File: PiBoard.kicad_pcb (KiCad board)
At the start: 4 copper layers, 90.1 x 92.5 mm, 128 parts, among them IC1 TCAN337DCNR, IC2 TPS2553QDBVRQ1, IC3 LM74502HDDFR, IC4 AP64501QSP-13, IC5 74LVC1G07QSE-7, IC6 TPS2553QDBVRQ1, IC7 TPS2553QDBVRQ1, J1 CarLVPowerConnector, J12 RTC Battery Port, J3 2222, J4 USB_C_Receptacle_USB2.0_16P, J5 USB_C_Receptacle_USB2.0_16P, J6 CarCANConnector, J7 Molex 470531000, J8 CarCANConnector, J9 HDMI_E, Q1 PSMN8R5-40MSDX, SW1 SW_Push, SW2 SW_Push, SW3 SW_Push, U1 RTC PCF8563T, U10 Fan PWM Controller, U13 CDSOT23-T24CAN, U14 MCP2515-E/STVAO, U3 FSUSB42MUX, Y4 8 MHz, Y6 ECS-.327-6

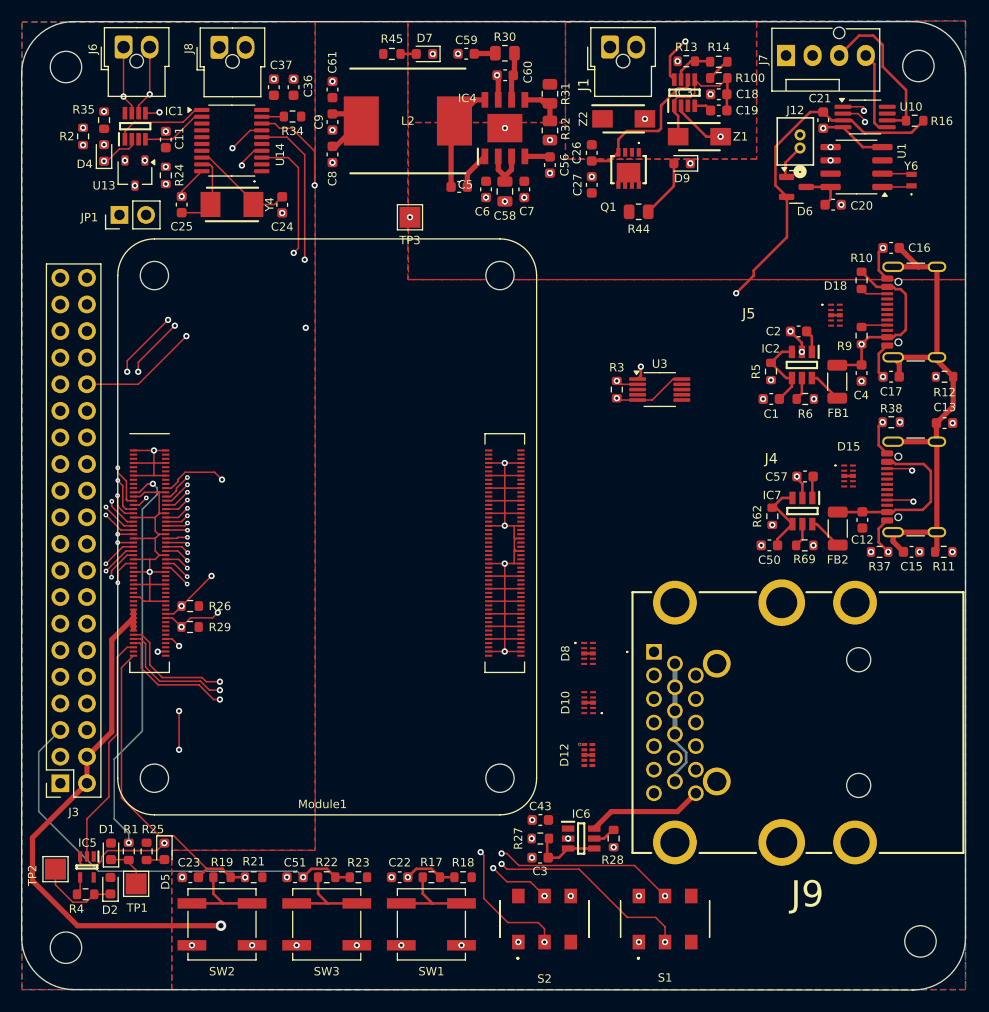
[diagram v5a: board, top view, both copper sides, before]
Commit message: ready to route high speed i believe
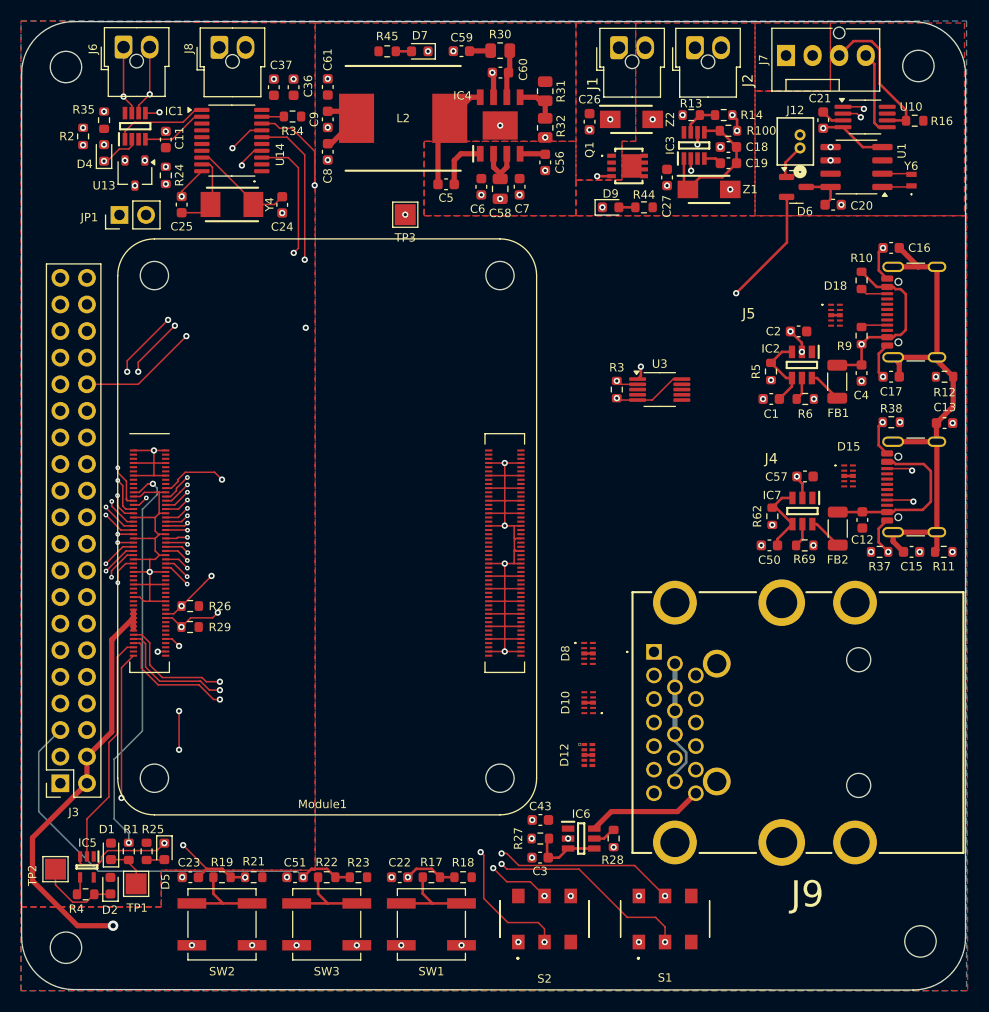
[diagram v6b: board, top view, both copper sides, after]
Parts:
- added J2: Display Breakout, UTSVT_Connectors:Molex_Nano-Fit_105309-xx02_1x02_P2.50mm_Vertical, F.Cu at (166.1, 53.8)
- R44: footprint Resistor_SMD:R_0805_2012Metric -> Resistor_SMD:R_0603_1608Metric
- moved D9 8.01 mm to (158.0, 69.0), turned to 0 degrees
- moved C27 7.22 mm to (163.4, 66.2), turned to -90 degrees
- moved R13 5.16 mm to (165.7, 60.2)
- moved IC3 5.12 mm to (166.0, 63.1)
- moved R100 5.12 mm to (169.3, 61.7), turned to 180 degrees
- moved C18 5.12 mm to (169.3, 63.2)
- moved C19 5.12 mm to (169.3, 64.8)
- moved Z1 5.12 mm to (167.4, 67.3)
- moved R14 5.11 mm to (168.8, 60.2)
- moved C26 2.98 mm to (156.0, 60.8)
- moved C5 1.27 mm to (142.3, 66.8)
- moved J1 0.86 mm to (158.8, 53.8)
- moved Z2 0.74 mm to (160.0, 60.6)
- moved R44 0.67 mm to (161.2, 69.0), turned to 180 degrees
- moved C56 0.51 mm to (151.8, 64.7)
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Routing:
- net +3.3V: track 80.2 -> 60.4 mm
- net +24V: track 22.0 -> 4.83 mm, vias 1 -> 0
- net +5V: track 61.6 -> 47.3 mm
- net GND: track 179.5 -> 175.4 mm, vias 70 -> 71
- net Net-(D9-A): track 5.64 -> 1.57 mm
- net Net-(IC3-GATE): track 14.8 -> 18.1 mm, vias 0 -> 3
- net /CM4 GPIO/SCL0: track 102.0 -> 99.3 mm
- net Net-(IC4-BST): track 3.61 -> 5.03 mm
- net /CM4 GPIO/SDA0: track 106.7 -> 105.3 mm
- net Net-(J7-Pin_3): track 15.3 -> 14.4 mm
- net /Power Distribution/LV+: track 2.29 -> 1.69 mm, vias 0 -> 3
- net Net-(IC3-OV): track 4.00 -> 3.46 mm
- net /Board_En: vias 4 -> 6
- added copper zone on In2.Cu, net /Power Distribution/LV+

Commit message: changed a bunch of stuff, still have work
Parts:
- removed C50, C57: 100n, Capacitor_SMD:C_0603_1608Metric
- removed IC7: TPS2553QDBVRQ1, Controls_Pi:SOT95P280X145-6N
- removed R62: 100n, Resistor_SMD:R_0603_1608Metric
- removed R69: 82k, Resistor_SMD:R_0603_1608Metric
- added C10: 120uF, Capacitor_SMD:C_0603_1608Metric, F.Cu at (179.7, 82.5)
- added C14: 100n, Capacitor_SMD:C_0603_1608Metric, F.Cu at (177.2, 98.9)
- added C28: 22uF, Capacitor_SMD:C_0603_1608Metric, F.Cu at (173.1, 96.5)
- added C29: 100uF, Capacitor_SMD:C_0805_2012Metric, F.Cu at (155.4, 125.2)
- added D11: VBUS_Debug LED, LED_SMD:LED_0603_1608Metric, F.Cu at (166.5, 102.3)
- added D3: VBUS_Hub LED, LED_SMD:LED_0603_1608Metric, F.Cu at (175.7, 90.0)
- added IC8: TPS25200DRVR, UTSVT_Power:SON65P200X200X80-7N, F.Cu at (173.1, 98.7)
- added R15: 33k, Resistor_SMD:R_0603_1608Metric, F.Cu at (169.9, 99.3)
- added R20: 100k, Resistor_SMD:R_0603_1608Metric, F.Cu at (175.6, 98.9)
- added R33: 100k, Resistor_SMD:R_0603_1608Metric, F.Cu at (173.0, 100.8)
- added R7: 1.5k, Resistor_SMD:R_0603_1608Metric, F.Cu at (179.0, 90.0)
- added R8: 1.5k, Resistor_SMD:R_0603_1608Metric, F.Cu at (169.7, 102.3)
- added TP4: TestPoint, TestPoint:TestPoint_Pad_2.0x2.0mm, F.Cu at (125.4, 128.5)
- C24, C25: value 22 pF -> 26 pF
- C6: value 100n -> 10uF
- R10, R9: value 5.1k -> 56k
- R5: value 100n -> 100k
- R6: value 82k -> 56k
- moved Y4 5.88 mm to (117.7, 64.6), turned to -90 degrees
- moved C24 5.14 mm to (121.9, 66.9), turned to 180 degrees
- moved C25 4.82 mm to (121.9, 68.5), turned to 180 degrees
- moved U14 2.31 mm to (124.2, 62.6)
- moved R34 1.54 mm to (128.9, 59.4), turned to 90 degrees
- moved D4 1.35 mm to (108.3, 63.8)
- moved R35 1.35 mm to (108.3, 60.7)
- moved R2 1.35 mm to (106.3, 62.2)
- moved C11 1.35 mm to (114.2, 62.5)
- moved IC1 1.35 mm to (111.3, 61.3)
- moved JP1 1.35 mm to (109.8, 69.7)
- moved U13 1.35 mm to (111.2, 65.7)
- moved R24 1.35 mm to (114.2, 66.0)
- moved R9 0.55 mm to (182.0, 81.8), turned to -90 degrees
- moved C36 0.47 mm to (127.3, 57.5)
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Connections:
- C4 pad 1: Net-(C4-Pad1) -> Net-(C10-Pad1)
- FB1 pad 2: Net-(C4-Pad1) -> Net-(C10-Pad1)
- J5 pad A4: Net-(C4-Pad1) -> Net-(C10-Pad1)
- J5 pad A9: Net-(C4-Pad1) -> Net-(C10-Pad1)
- J5 pad B4: Net-(C4-Pad1) -> Net-(C10-Pad1)
- J5 pad B9: Net-(C4-Pad1) -> Net-(C10-Pad1)
- Module1 pad 88: unconnected-(Module1A-+1.8v_(Output)-Pad88) -> +1.8V
- Module1 pad 90: unconnected-(Module1A-+1.8v_(Output)-Pad90) -> +1.8V
- R10 pad 1: Net-(C4-Pad1) -> +5V
- R9 pad 1: Net-(C4-Pad1) -> +5V
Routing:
- net +3.3V: track 60.4 -> 90.1 mm, vias 3 -> 4
- net +1.8V: track 0.00 -> 26.8 mm
- net Net-(C4-Pad1): track 17.6 -> 0.00 mm, vias 1 -> 0
- net Net-(C10-Pad1): track 0.00 -> 15.8 mm
- net /USB2.0 high speed/VBUS_Debug: track 3.25 -> 16.8 mm
- net Net-(IC7-EN): track 7.51 -> 0.00 mm
- net /CM4 GPIO/CAN_SPI_MISO: track 86.5 -> 92.3 mm
- net /CarCAN/CAN_RX: track 6.28 -> 9.96 mm
- net /CarCAN/CAN_TX: track 8.94 -> 12.6 mm
- net Net-(J5-CC1): track 2.52 -> 5.59 mm, vias 0 -> 2
- net /Board_En: track 129.2 -> 126.2 mm, vias 6 -> 5
- net /USB2.0 high speed/VBUS_Hub: track 3.22 -> 6.08 mm
- net /HDMI and High Speed/HDMI_5V: track 11.1 -> 13.6 mm
- net Net-(IC7-ILIM): track 2.28 -> 0.00 mm
- net /CM4 GPIO/CAN_INTR: track 51.8 -> 49.8 mm
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
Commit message: poop
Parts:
- removed C14: 100n, Capacitor_SMD:C_0603_1608Metric
- removed C28: 22uF, Capacitor_SMD:C_0603_1608Metric
- removed IC8: TPS25200DRVR, UTSVT_Power:SON65P200X200X80-7N
- added C30: 100n, Capacitor_SMD:C_0603_1608Metric, F.Cu at (177.4, 98.8)
- added C31: 100n, Capacitor_SMD:C_0603_1608Metric, F.Cu at (170.7, 97.8)
- added D13: HBT, LED_SMD:LED_0603_1608Metric, F.Cu at (159.7, 76.4)
- added D14: FAULT, LED_SMD:LED_0603_1608Metric, F.Cu at (159.7, 74.7)
- added D16: STUFF, LED_SMD:LED_0603_1608Metric, F.Cu at (159.7, 78.1)
- added IC7: TPS2553QDBVRQ1, Controls_Pi:SOT95P280X145-6N, F.Cu at (174.4, 98.5)
- added R36: 0, Resistor_SMD:R_0603_1608Metric, F.Cu at (174.3, 101.1)
- added R39: 100k, Resistor_SMD:R_0603_1608Metric, F.Cu at (170.7, 96.2)
- added R40: 56k, Resistor_SMD:R_0603_1608Metric, F.Cu at (170.7, 99.6)
- R15: value 33k -> 700
- R20, R33: value 100k -> 700
- moved R20 30.8 mm to (156.5, 74.7), turned to 180 degrees
- moved R33 28.1 mm to (156.5, 78.1), turned to 180 degrees
- moved R15 26.6 mm to (156.5, 76.4), turned to 180 degrees
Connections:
- R15 pad 1: GND -> Net-(D13-K)
- R15 pad 2: Net-(IC8-ILIM) -> /CM4 GPIO/GPIO19
- R20 pad 2: /USB2.0 high speed/VBUS_Debug -> /CM4 GPIO/GPIO13
- R33 pad 2: +3.3V -> /CM4 GPIO/GPIO26
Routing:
- net /CM4 GPIO/GPIO26: track 36.0 -> 84.3 mm, vias 1 -> 5
- net /CM4 GPIO/GPIO19: track 40.6 -> 87.5 mm, vias 1 -> 5
- net /CM4 GPIO/GPIO13: track 45.4 -> 91.1 mm, vias 1 -> 5
- net +3.3V: track 90.1 -> 79.0 mm, vias 4 -> 5
- net /Board_En: track 126.2 -> 135.4 mm, vias 5 -> 6
- net Net-(IC7-EN): track 0.00 -> 6.04 mm
- net GND: track 173.7 -> 168.5 mm
- net Net-(IC7-ILIM): track 0.00 -> 2.44 mm
- net Net-(D13-K): track 0.00 -> 1.59 mm
- net Net-(IC8-ILIM): track 1.57 -> 0.00 mm
- net /USB2.0 high speed/VBUS_Debug: track 16.8 -> 16.3 mm
